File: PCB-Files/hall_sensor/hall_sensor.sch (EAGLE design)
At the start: 5 parts

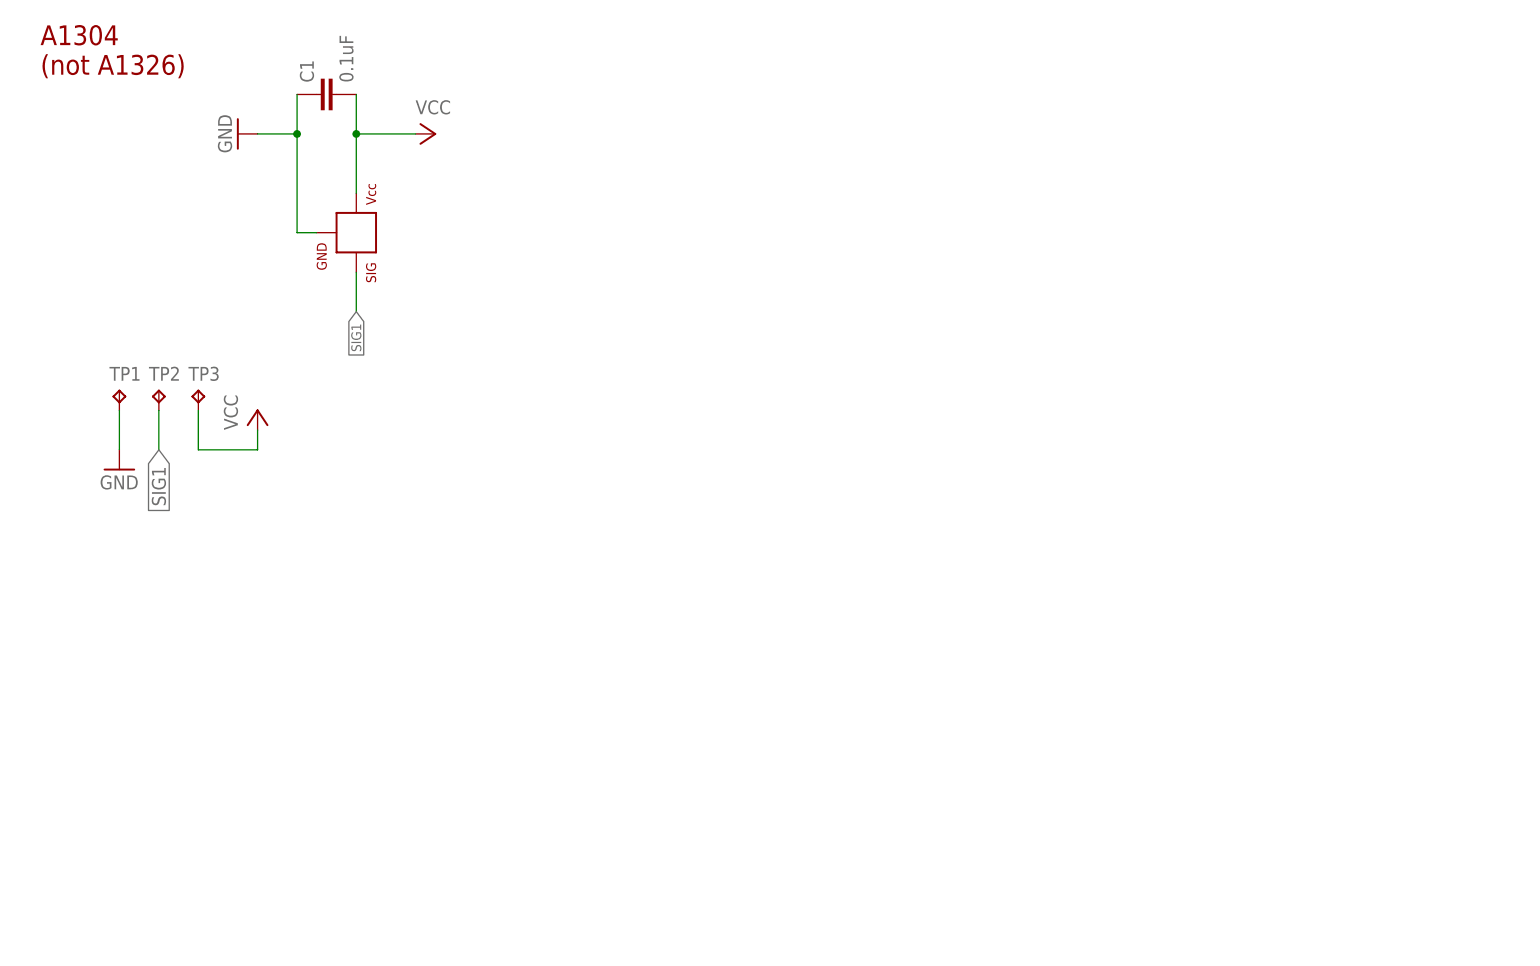
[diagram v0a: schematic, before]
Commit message: esp32 touch sketch tests
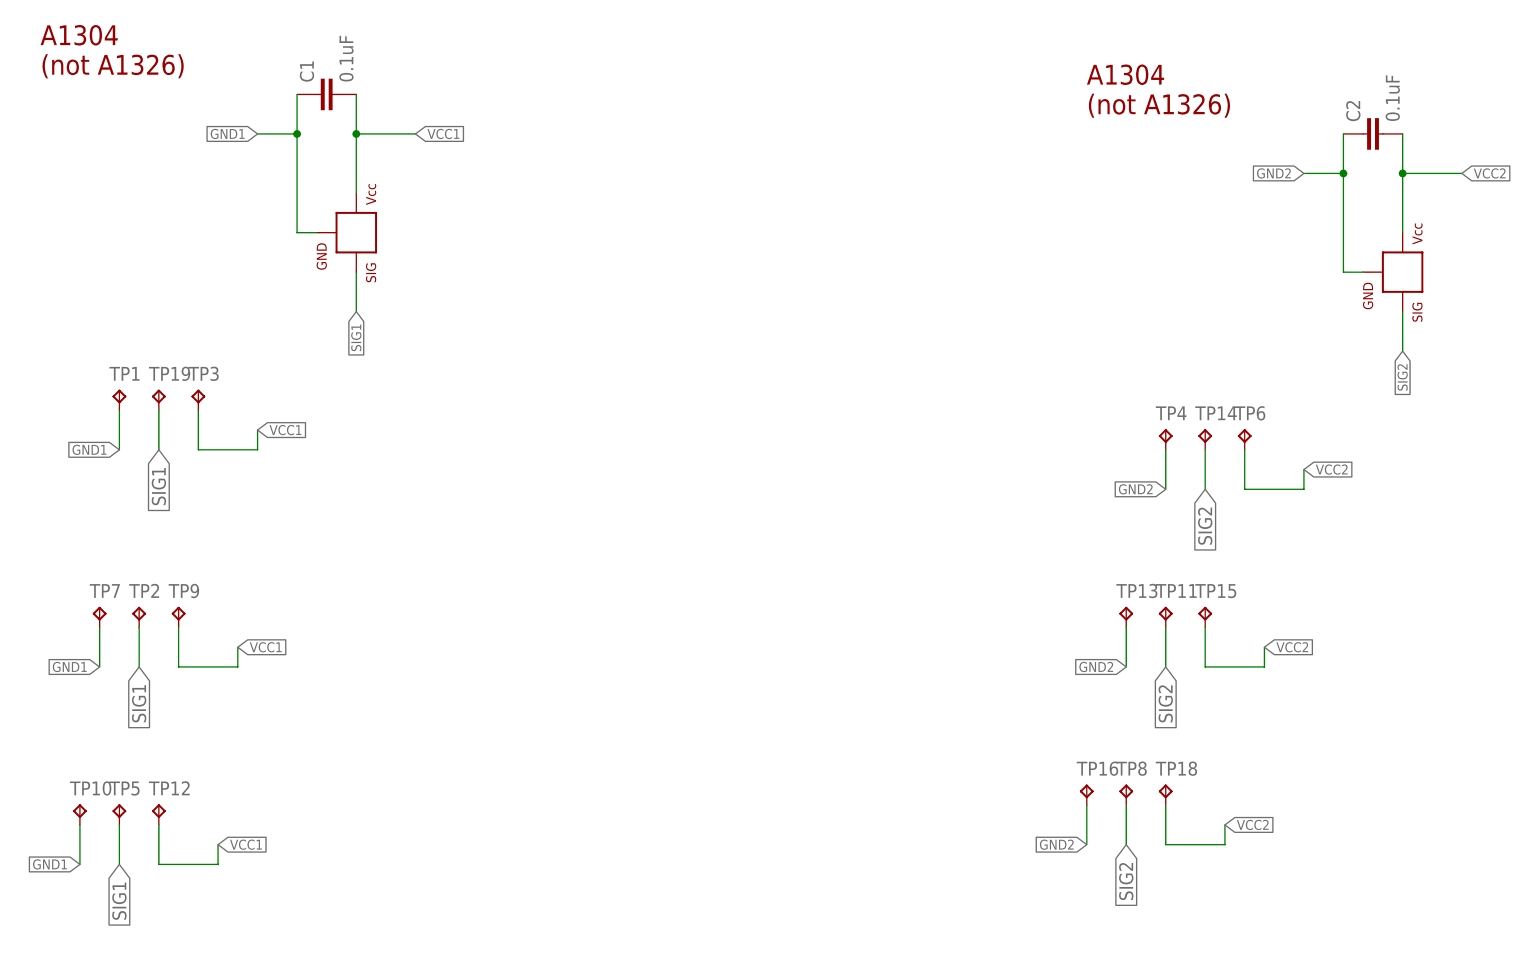
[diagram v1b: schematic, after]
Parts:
- added C2: 0.1uF, SparkFun:CAP0603-CAP
- added HALL1: HALLEFFECT-A1326, Andy_Sigler:HALLEFFECT-A1326
- added TP10, TP12, TP13, TP15, TP16, TP18, TP4, TP6, TP7, TP9: TPTP10SQ, testpad:TPTP10SQ
- added TP11, TP14, TP19, TP5, TP8: TPTP15R, testpad:TPTP15R
- TP2: value TPTP10SQ -> TPTP15R; device testpad:TPTP10SQ -> testpad:TPTP15R
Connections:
- removed net GND: C1.1, HALL.GND, TP1.TP
- removed net VCC: C1.2, HALL.VCC, TP3.TP
- new net GND1: C1.1, HALL.GND, TP1.TP, TP10.TP, TP7.TP
- new net GND2: C2.1, HALL1.GND, TP13.TP, TP16.TP, TP4.TP
- new net SIG2: HALL1.SIG, TP11.TP, TP14.TP, TP8.TP
- new net VCC1: C1.2, HALL.VCC, TP12.TP, TP3.TP, TP9.TP
- new net VCC2: C2.2, HALL1.VCC, TP15.TP, TP18.TP, TP6.TP
- net SIG1: now also TP19.TP, TP5.TP
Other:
- moved on the sheet: TP2
